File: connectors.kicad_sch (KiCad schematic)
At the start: 33 parts, among them J10 Conn_01x06, J11 Conn_01x04, J12 USB_C_Receptacle_USB2.0_16P, J14 Conn_01x03, J6 FTSH-107-01-L-DV-K-TR, J7 Conn_01x03, J8 Conn_01x02, J9 Conn_01x07, Q7 AO3400A, Q8 AO3400A

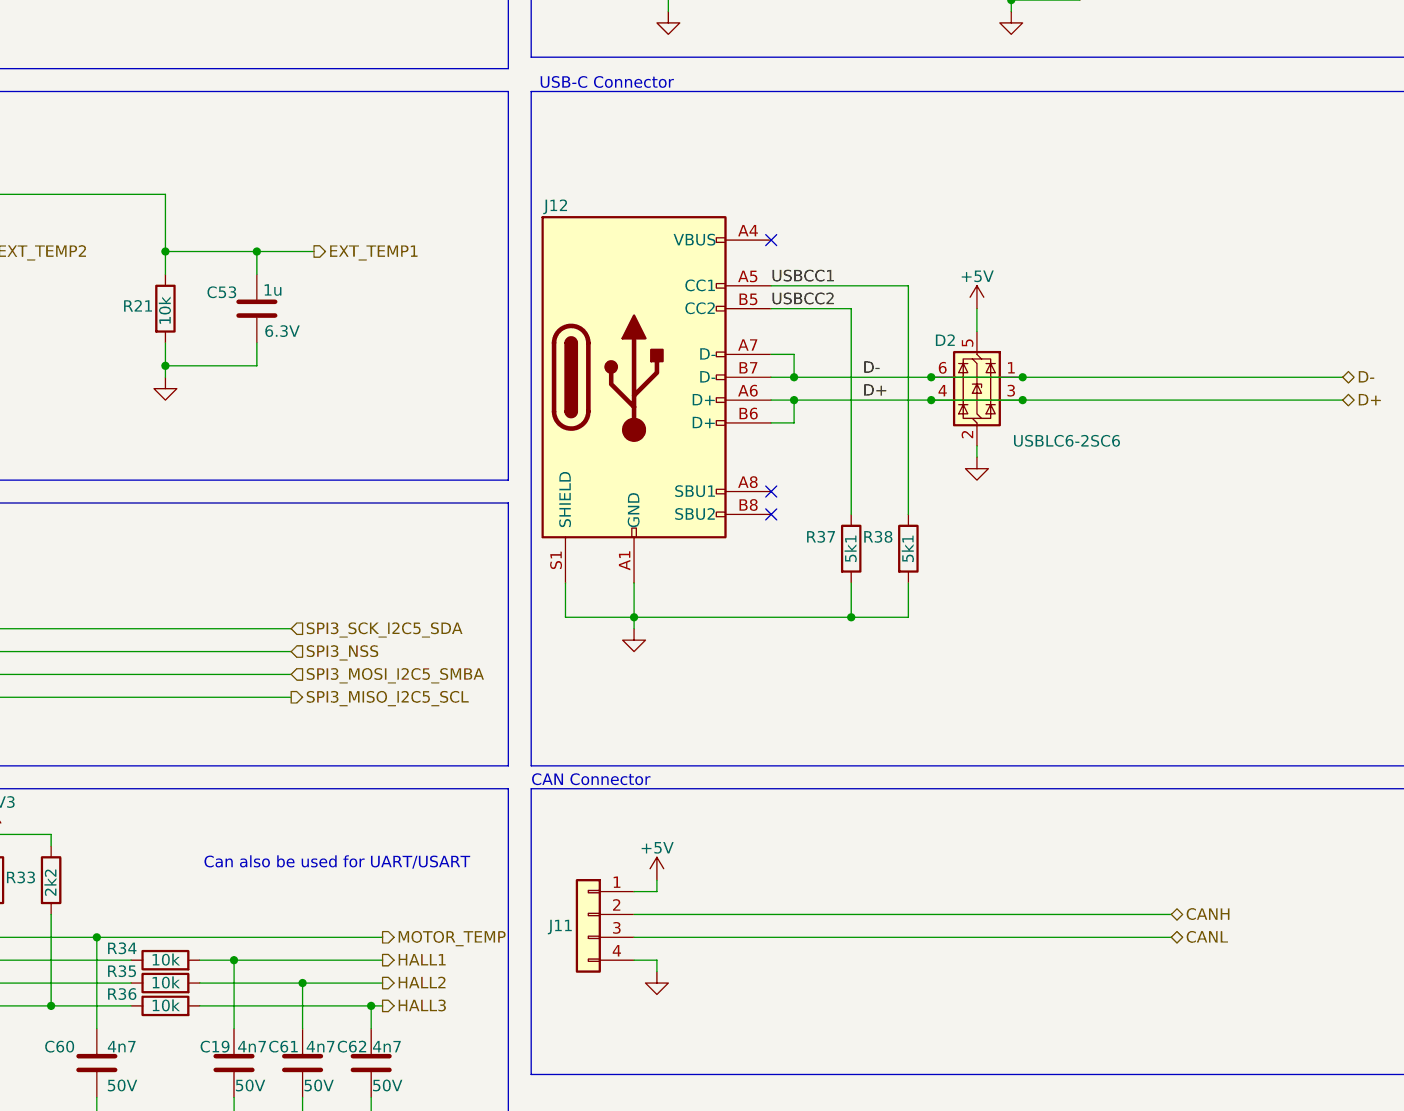
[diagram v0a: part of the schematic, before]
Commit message: added leds and buttons
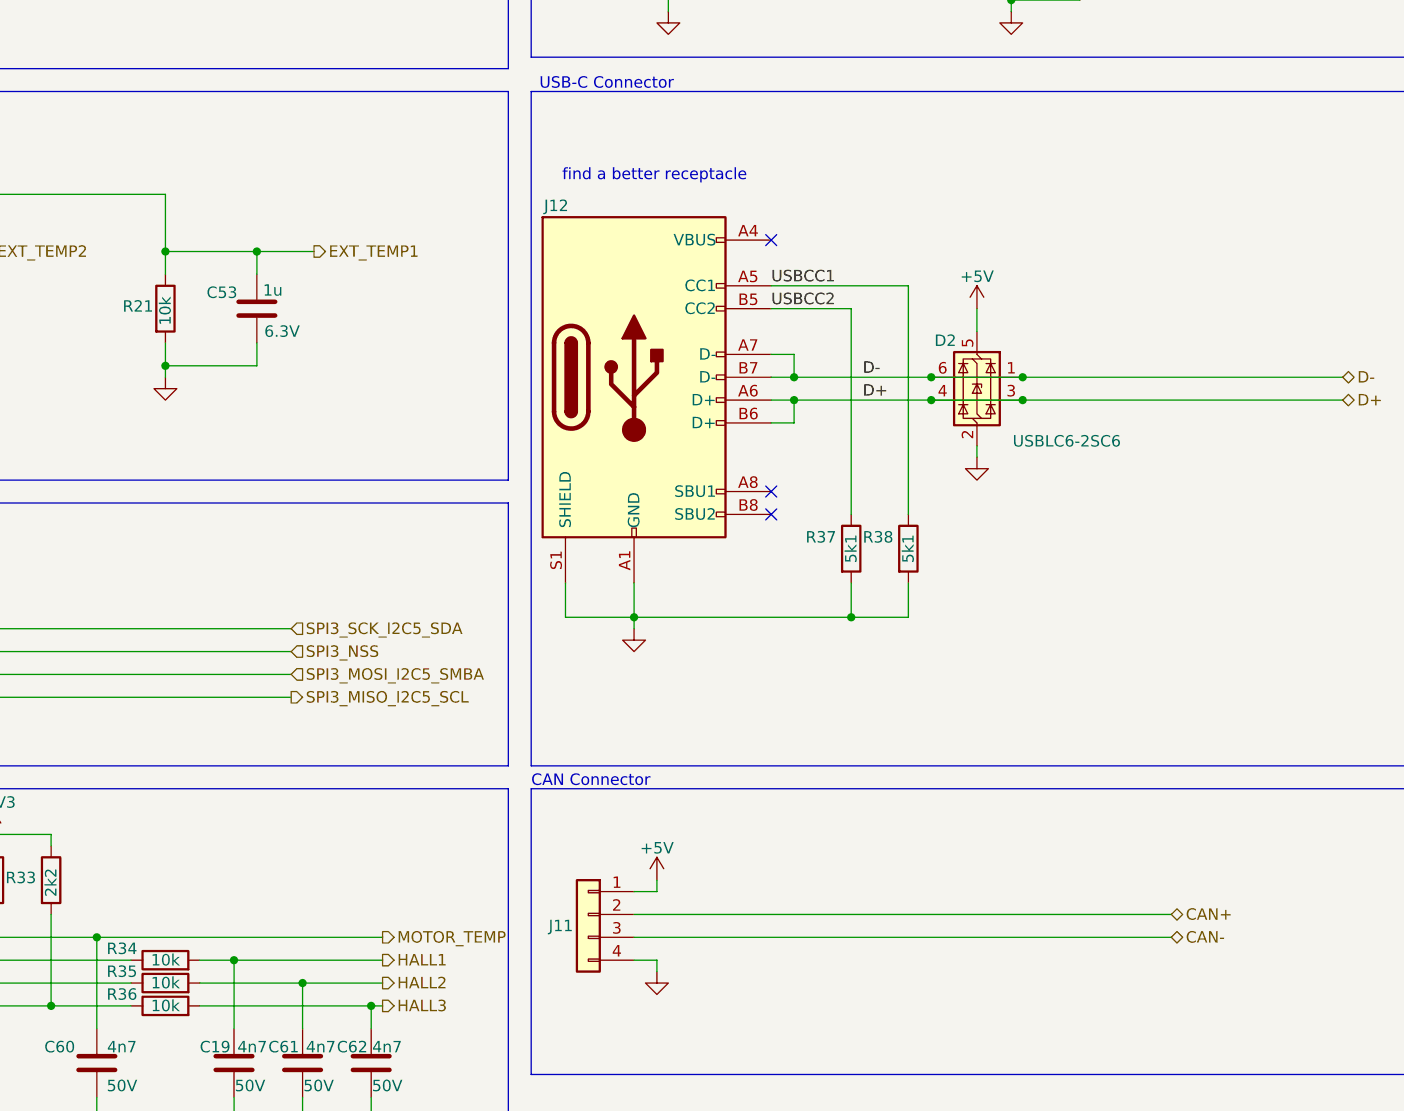
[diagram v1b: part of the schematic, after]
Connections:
- net CANH renamed CAN+
- net CANL renamed CAN-
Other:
- note added: "find a better receptacle"
- note removed: "Can also be used for UART/USART"
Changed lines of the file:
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@@
 		)
 	)
-	(text "tau = R*C = 1k * 630pf = 630ns"
+	(text "find a better receptacle\n"
 		(exclude_from_sim no)
-		(at 137.16 39.878 0)
+		(at 117.856 62.738 0)
 		(effects
 			(font
@@
 		)
 	)
-	(text "External Temp. Readings"
+	(text "tau = R*C = 1k * 630pf = 630ns"
 		(exclude_from_sim no)
-		(at 27.178 52.578 0)
+		(at 137.16 39.878 0)
 		(effects
 			(font
@@
 		)
 	)
-	(text "Servo"
+	(text "External Temp. Readings"
 		(exclude_from_sim no)
-		(at 204.216 14.478 0)
+		(at 27.178 52.578 0)
 		(effects
 			(font
 				(size 1.27 1.27)
 			)
-			(justify left)
 		)
 	)
-	(text "Can also be used for UART/USART"
+	(text "Servo"
 		(exclude_from_sim no)
-		(at 82.55 139.192 0)
+		(at 204.216 14.478 0)
 		(effects
 			(font
 				(size 1.27 1.27)
 			)
+			(justify left)
 		)
 	)
@@
 		)
 	)
-	(hierarchical_label "CANL"
+	(hierarchical_label "CAN-"
 		(shape bidirectional)
 		(at 175.26 147.32 0)
@@
 		)
 	)
-	(hierarchical_label "CANH"
+	(hierarchical_label "CAN+"
 		(shape bidirectional)
 		(at 175.26 144.78 0)

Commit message: schematic and PCB reviews are done, ready for release and first order.
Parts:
- removed J12: USB_C_Receptacle_USB2.0_16P, Connector_USB:USB_C_Receptacle_GCT_USB4105-xx-A_16P_TopMnt_Horizontal, symbol Connector:USB_C_Receptacle_USB2.0_16P
- added J12: USB_C_Receptacle_USB2.0_16P, NanoGaN:USB_C_Receptacle_GCT_USB4105-xx-A_16P_TopMnt_Horizontal, symbol NanoGaN:USB_C_Receptacle_USB2.0_16P
- Q7: LCSC (none) -> C20917
- R29, R31, R33: value 0402WGF1001TCE -> 0402WGF2201TCE; LCSC C11702 -> C25879
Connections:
- net D+: now also J12.A6 (D+), J12.B6 (D+)
- net D-: now also J12.A7 (D-), J12.B7 (D-)
- net GND: now also J12.A1 (GND), J12.A12 (GND), J12.B1 (GND), J12.B12 (GND), J12.S1 (SHIELD)
- net USBCC1: now also J12.A5 (CC1)
- net USBCC2: now also J12.B5 (CC2)
- new net: J12.A4 (VBUS), J12.A9 (VBUS)
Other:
- note removed: "find a better receptacle"
- company: (none) -> Eren Akbayin
- title: (none) -> NanoGaN
- moved on the sheet: R37, R38
